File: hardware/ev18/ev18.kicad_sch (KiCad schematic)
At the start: 206 parts, among them CN1 Conn_05x02_Female, CN2 PJ-242, J1 USB_C_Receptacle, J10 Conn_02x05_Counter_Clockwise, J11 Conn_02x05_Counter_Clockwise, J12 Conn_01x01, J13 Conn_01x01, J14 Conn_01x01, J15 Conn_01x01, J16 Conn_01x01, J17 Conn_01x01, J18 Conn_01x01, J19 Conn_01x01, J2 Conn_01x02_Socket, J20 Conn_02x05_Counter_Clockwise, J21 Conn_01x01, J22 USB_C_Receptacle, J23 Conn_01x01, J3 AudioJack4, J4 Conn_02x03_Odd_Even, J5 Conn_02x03_Odd_Even, J6 Conn_02x05_Counter_Clockwise, J7 Conn_02x05_Counter_Clockwise, J8 Conn_02x05_Counter_Clockwise, J9 Conn_02x05_Counter_Clockwise, Q1 2N7002, Q2 2N7002, Q3 2N7002, SW1 SW_SPDT, SW2 SW_Push, SW3 SW_Push, SW4 SW_Push, SW5 SW_Push, SW6 SW_Push, SW7 SW_Push, U1 BQ21040DBV, U10 STM32F405RGTx, U11 USBLC6-2P6, U12 XC6227C301MR-G, U2 USBLC6-2P6, U3 STM32F072CBTx, U4 CH340C, U5 TPS63060, U6 WM8960CGEFL/RV, U7 ESP32-S3-WROOM-1, U8 M24C02-RMN6TP, U9 TPS2116DRL, Y1 Crystal_GND24

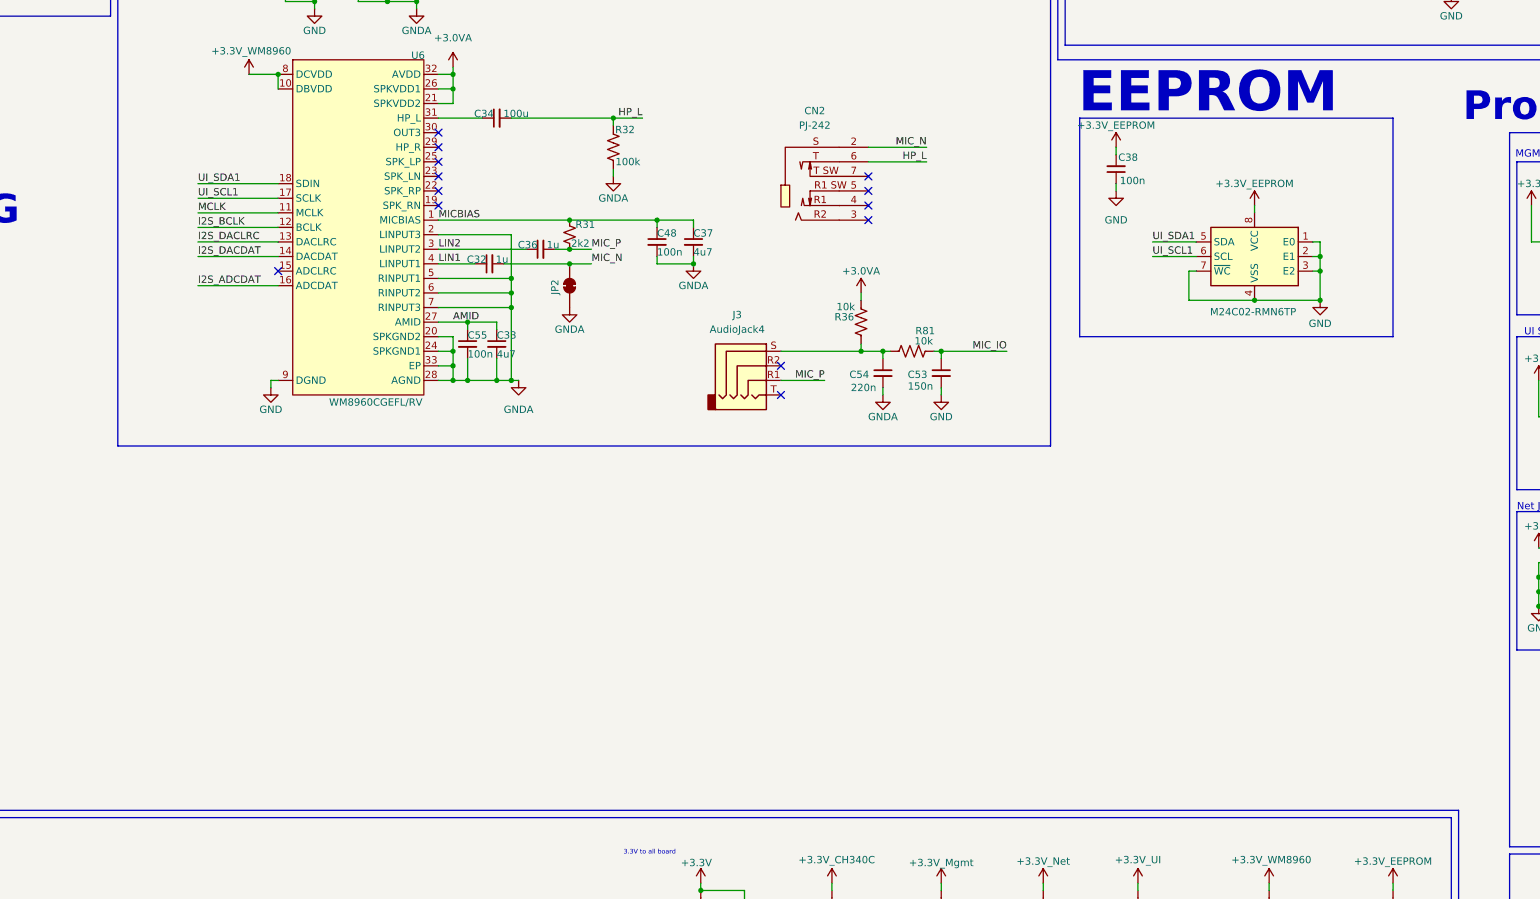
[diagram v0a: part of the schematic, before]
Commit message: update schematic to have mic design for reference
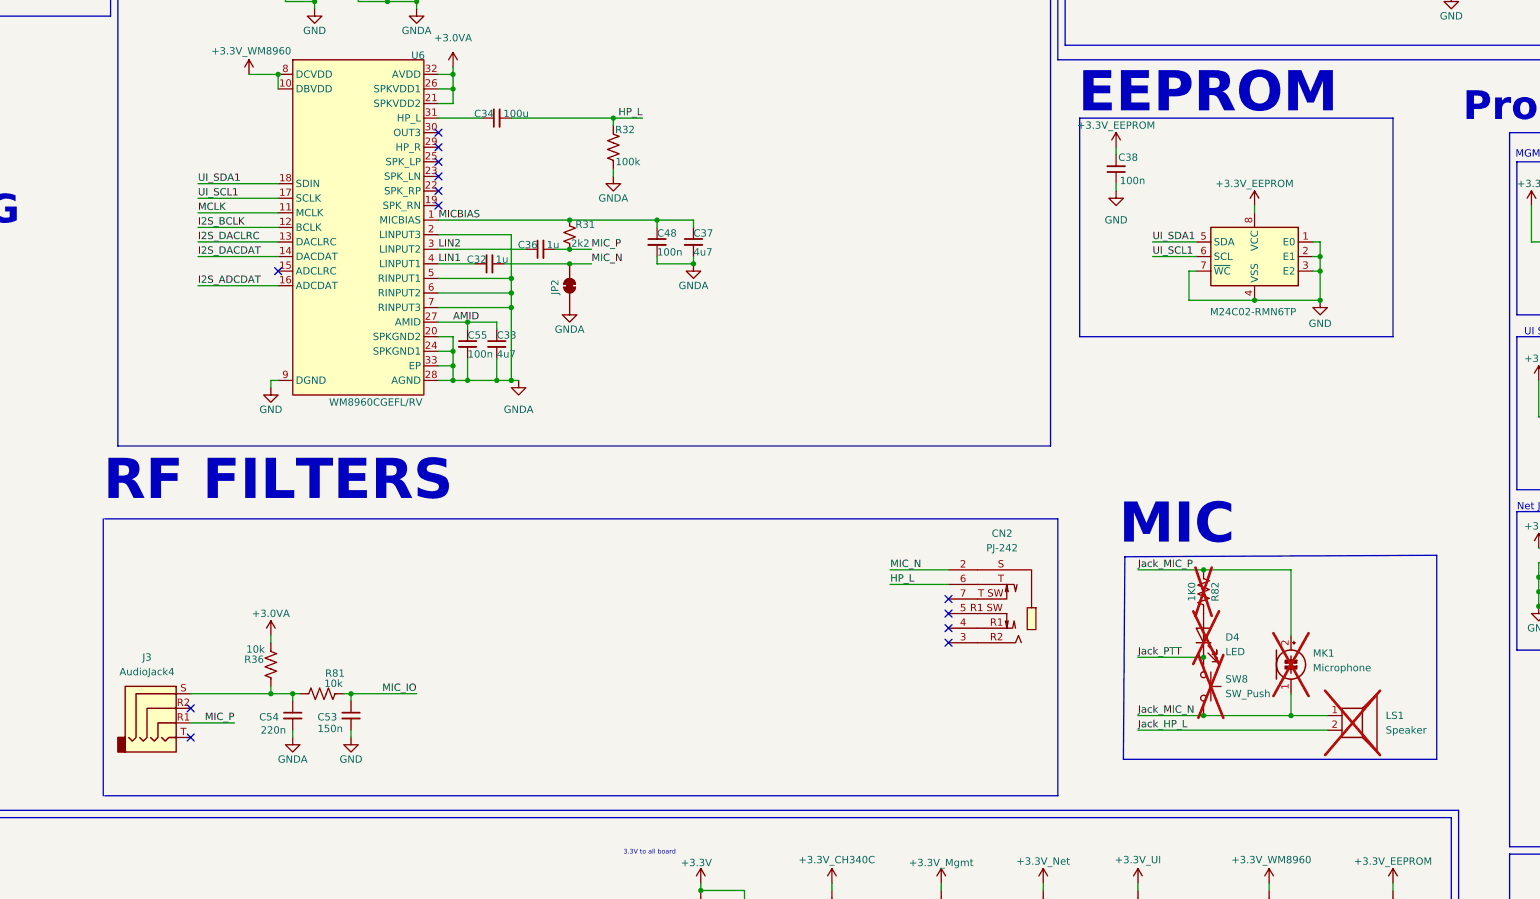
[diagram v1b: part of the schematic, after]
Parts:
- added D4: LED, symbol Device:LED
- added LS1: Speaker, symbol Device:Speaker
- added MK1: Microphone, symbol Device:Microphone_Condenser
- added R82: 1K0, symbol Device:R_US
- added SW8: SW_Push, symbol Switch:SW_Push
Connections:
- new net: D4.2 (A), R82.2
- new net Jack_HP_L: LS1.2
- new net Jack_MIC_N: LS1.1, MK1.1 (-), SW8.2
- new net Jack_MIC_P: MK1.2 (+), R82.1
- new net Jack_PTT: D4.1 (K), SW8.1
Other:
- note added: "MIC"
- note added: "RF FILTERS"
- moved on the sheet: C53, C54, CN2, J3, R36, R81

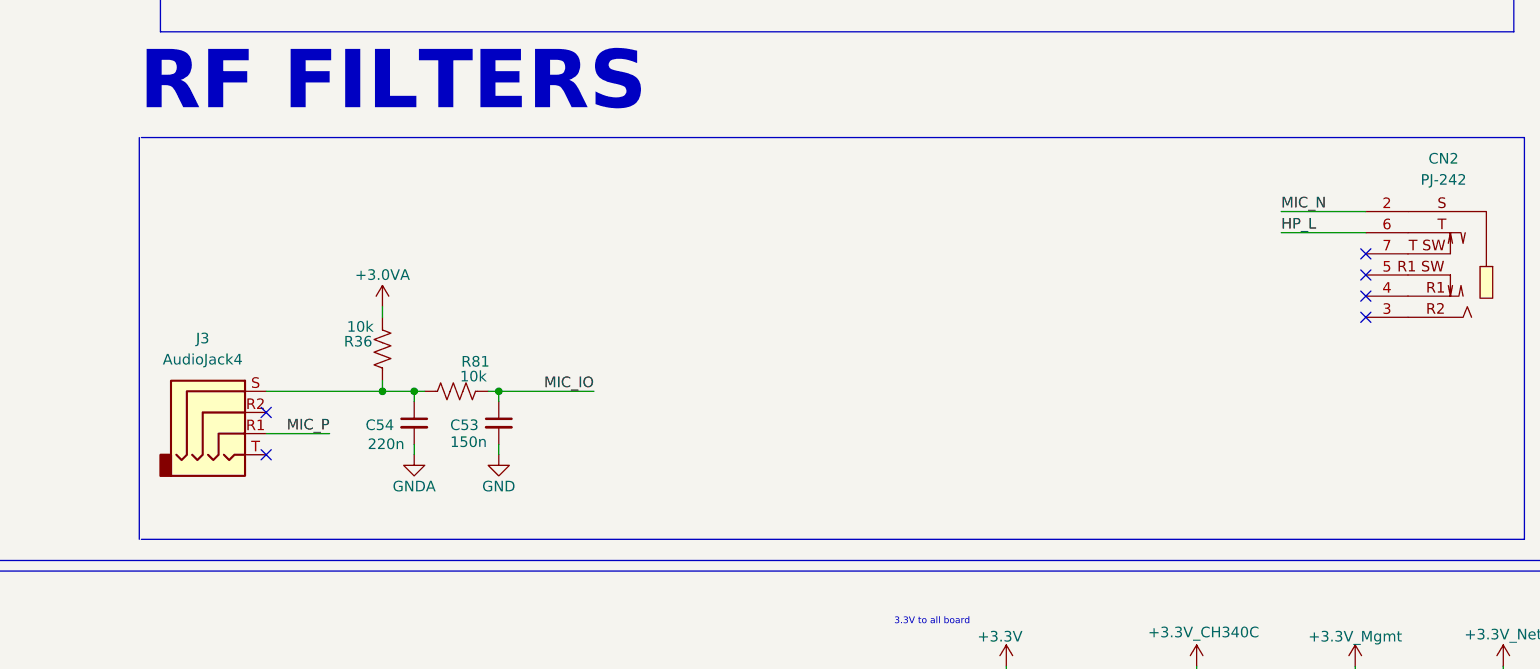
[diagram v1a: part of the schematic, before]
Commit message: start RF filters
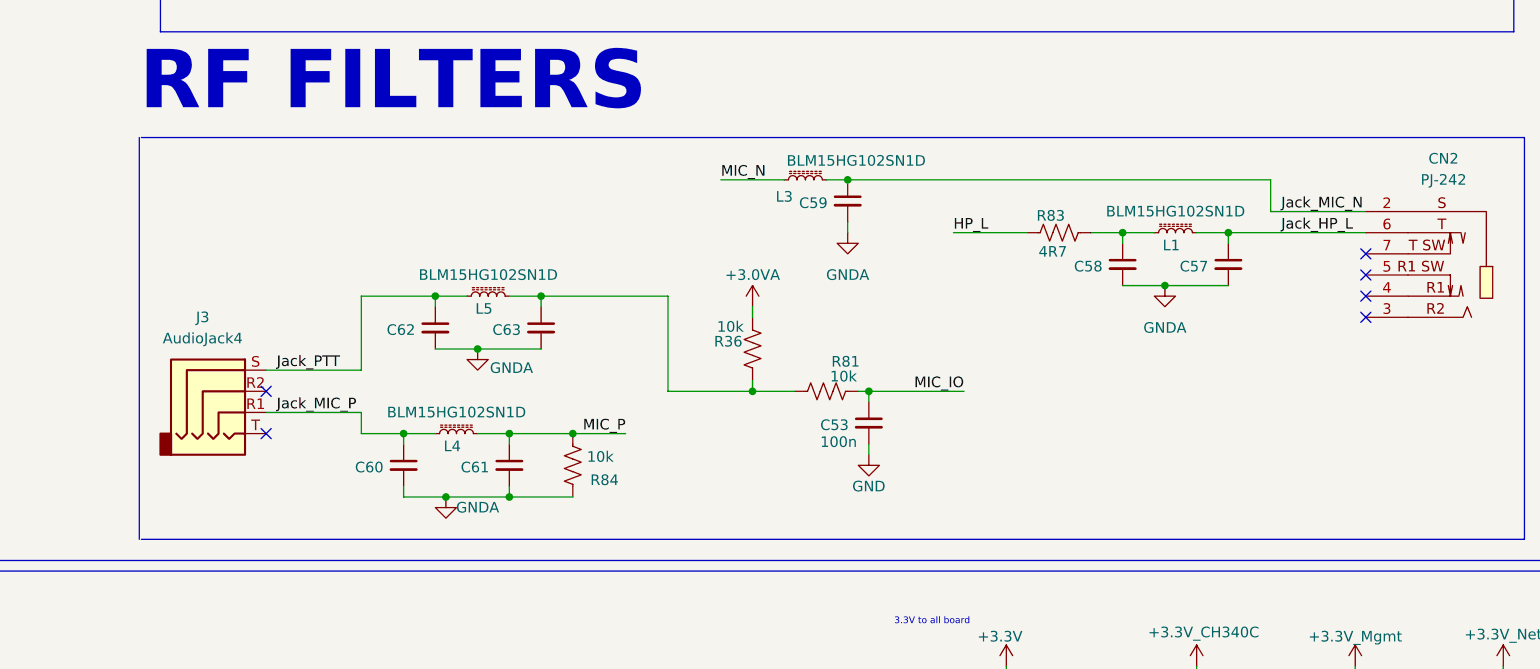
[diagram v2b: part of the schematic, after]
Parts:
- removed C54: 220n, Capacitor_SMD:C_0402_1005Metric, symbol Device:C_Small
- added C57, C58, C59, C60, C61, C62, C63: ~, Capacitor_SMD:C_0402_1005Metric, symbol Device:C_Small
- added L1, L3, L4, L5: BLM15HG102SN1D, Inductor_SMD:L_0402_1005Metric, symbol Device:L_Ferrite_Small
- added R83: 4R7, Resistor_SMD:R_0402_1005Metric, symbol Device:R_US
- added R84: 10k, Resistor_SMD:R_0402_1005Metric, symbol Device:R_US
- C53: value 150n -> 100n; JLCPCB Part # C505466 -> (none)
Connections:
- net GNDA: now also C57.2, C58.2, C59.2, C60.2, C61.2, C62.2, C63.2, R84.1
- net HP_L: now also R83.1; no longer CN2.6
- net Jack_HP_L: now also CN2.6, C57.1, L1.2
- net Jack_MIC_N: now also CN2.2, C59.1, L3.2
- net Jack_MIC_P: now also J3.R1, C60.1, L4.1
- net Jack_PTT: now also J3.S, C62.1, L5.1
- net MIC_N: now also L3.1; no longer CN2.2
- net MIC_P: now also C61.1, L4.2, R84.2; no longer J3.R1
- net at R36.1, R81.1: now also C63.1, L5.2; no longer J3.S
- new net: C58.1, L1.1, R83.2
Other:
- moved on the sheet: C53, J3, R36, R81

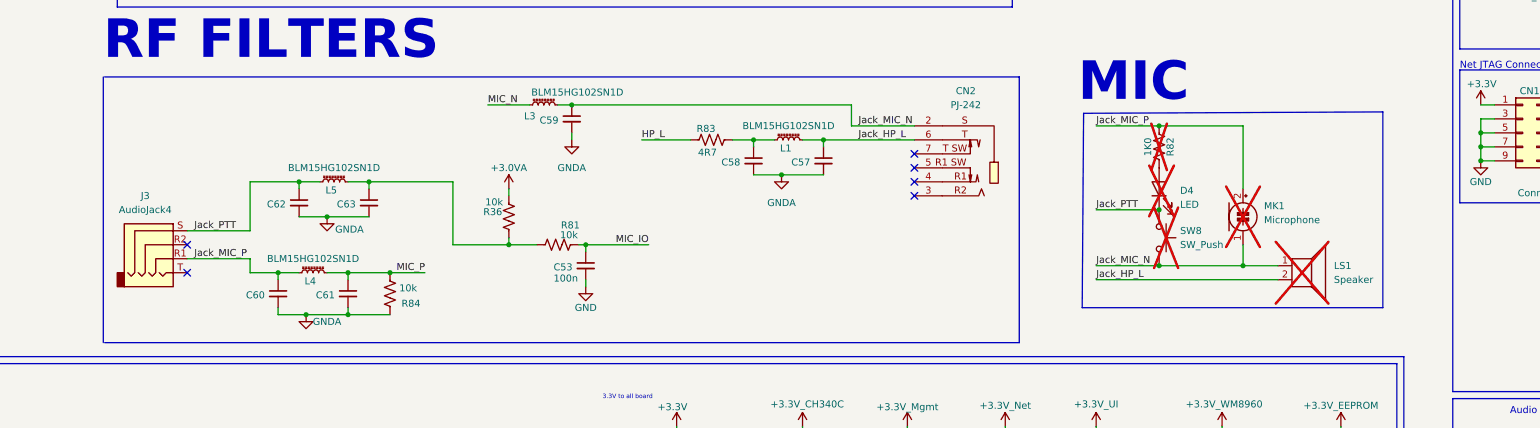
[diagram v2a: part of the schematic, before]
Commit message: update filter cap values
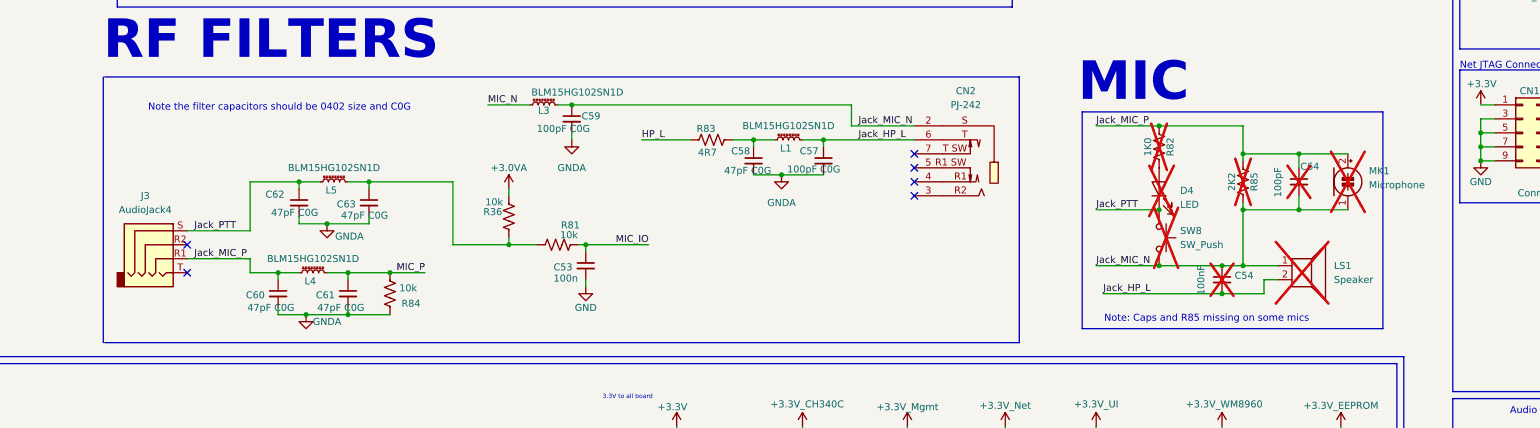
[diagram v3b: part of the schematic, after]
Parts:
- added C54: 100nF, symbol Device:C_Small
- added C64: 100pF, symbol Device:C_Small
- added R85: 2K2, symbol Device:R_US
- C57, C59: value ~ -> 100pF C0G
- C58, C60, C61, C62, C63: value ~ -> 47pF C0G
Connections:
- net Jack_HP_L: now also C54.2
- net Jack_MIC_N: now also C54.1, C64.2, R85.2
- net Jack_MIC_P: now also C64.1, R85.1
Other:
- note added: "Note the filter capacitors should be 0402 size and C0G"
- note added: "Note: Caps and R85 missing on some mics"
- moved on the sheet: MK1

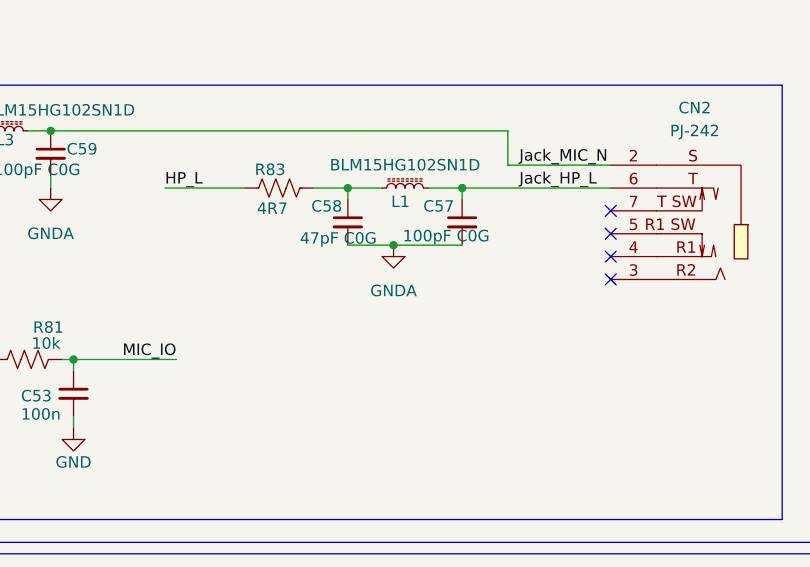
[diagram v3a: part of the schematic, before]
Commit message: update schematic date
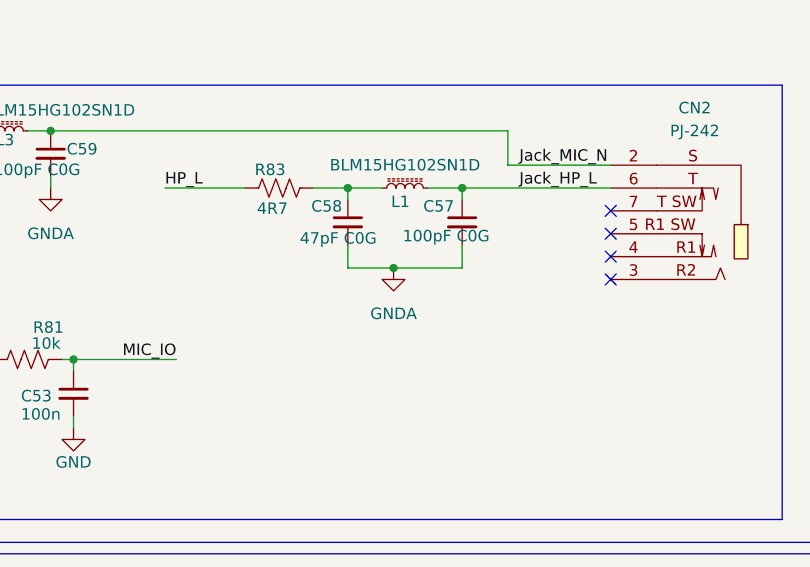
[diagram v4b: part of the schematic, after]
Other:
- title: EV17MK1 FINN BERG & BRETT REGNIER -> EV18MK1 FINN BERG & BRETT REGNIER
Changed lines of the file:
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@@
 	(paper "A2")
 	(title_block
-		(title "EV17MK1 FINN BERG & BRETT REGNIER")
-		(date "2026-03-06")
-		(rev "EV17MK1")
+		(title "EV18MK1 FINN BERG & BRETT REGNIER")
+		(date "2026-05-31")
+		(rev "EV18MK1")
 		(company "CISCO SYSTEMS INC")
 	)
@@
 	)
 	(junction
-		(at 332.74 265.43)
-		(diameter 0)
-		(color 0 0 0 0)
-	)
-	(junction
 		(at 288.29 322.58)
 		(diameter 0)
@@
 	)
 	(junction
+		(at 332.74 267.97)
+		(diameter 0)
+		(color 0 0 0 0)
+	)
+	(junction
 		(at 93.98 328.93)
 		(diameter 0)
@@
 	(wire
 		(pts
-			(xy 327.66 265.43) (xy 332.74 265.43)
+			(xy 327.66 267.97) (xy 332.74 267.97)
 		)
 		(stroke
@@
 	(wire
 		(pts
+			(xy 340.36 267.97) (xy 340.36 265.43)
+		)
+		(stroke
+			(width 0)
+			(type default)
+		)
+	)
+	(wire
+		(pts
 			(xy 232.41 106.68) (xy 247.65 106.68)
 		)
@@
 	(wire
 		(pts
-			(xy 332.74 265.43) (xy 340.36 265.43)
+			(xy 332.74 267.97) (xy 340.36 267.97)
 		)
 		(stroke
@@
 	(wire
 		(pts
+			(xy 327.66 267.97) (xy 327.66 265.43)
+		)
+		(stroke
+			(width 0)
+			(type default)
+		)
+	)
+	(wire
+		(pts
 			(xy 35.56 54.61) (xy 35.56 55.88)
 		)
@@
 	(symbol
 		(lib_id "power:GNDA")
-		(at 332.74 265.43 0)
+		(at 332.74 267.97 0)
 		(unit 1)
 		(exclude_from_sim no)
@@
 		(fields_autoplaced yes)
 		(property "Reference" "#PWR0112"
-			(at 332.74 271.78 0)
+			(at 332.74 274.32 0)
 			(effects
 				(font
@@
 		)
 		(property "Value" "GNDA"
-			(at 332.74 270.51 0)
+			(at 332.74 273.05 0)
 			(effects
 				(font
@@
 		)
 		(property "Footprint" ""
-			(at 332.74 265.43 0)
+			(at 332.74 267.97 0)
 			(effects
 				(font
@@
 		)
 		(property "Datasheet" ""
-			(at 332.74 265.43 0)
+			(at 332.74 267.97 0)
 			(effects
 				(font
@@
 		)
 		(property "Description" "Power symbol creates a global label with name \"GNDA\" , analog ground"
-			(at 332.74 265.43 0)
+			(at 332.74 267.97 0)
 			(effects
 				(font
